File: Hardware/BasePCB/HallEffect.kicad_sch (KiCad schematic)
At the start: 4 parts, among them IC3 TMCS1123C1AQDVGR

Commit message: add JLC p/n
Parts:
- C5: Assemble (none) -> Y; LSCC P/N (none) -> C14663
- IC3: Assemble (none) -> Y; LSCC P/N (none) -> C22445470
- R2: Assemble (none) -> Y; LSCC P/N (none) -> C25804
- TP27: Assemble (none) -> N
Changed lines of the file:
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@@
+			)
+		)
+		(property "LSCC P/N" ""
+			(at 149.86 77.47 0)
+			(effects
+				(font
+					(size 1.27 1.27)
+				)
+				(hide yes)
+			)
+		)
+		(property "Assemble" "N"
+			(at 149.86 77.47 0)
+			(effects
+				(font
+					(size 1.27 1.27)
+				)
+				(hide yes)
 			)
 		)
@@
 		)
 		(property "P/N" "MLASH168SB7104KTNA01"
+			(at 76.2 81.28 0)
+			(effects
+				(font
+					(size 1.27 1.27)
+				)
+				(hide yes)
+			)
+		)
+		(property "LSCC P/N" "C14663"
+			(at 76.2 81.28 0)
+			(effects
+				(font
+					(size 1.27 1.27)
+				)
+				(hide yes)
+			)
+		)
+		(property "Assemble" "Y"
 			(at 76.2 81.28 0)
 			(effects
@@
 			)
 		)
+		(property "LSCC P/N" "C22445470"
+			(at 104.14 72.39 0)
+			(effects
+				(font
+					(size 1.27 1.27)
+				)
+				(hide yes)
+			)
+		)
+		(property "Assemble" "Y"
+			(at 104.14 72.39 0)
+			(effects
+				(font
+					(size 1.27 1.27)
+				)
+				(hide yes)
+			)
+		)
 		(pin "7"
 		)
@@
 			(at 87.63 81.28 0)
 			(effects
+				(font
+					(size 1.27 1.27)
+				)
+				(hide yes)
+			)
+		)
+		(property "LSCC P/N" "C25804"
+			(at 87.63 81.28 0)
+			(effects
+				(font
+					(size 1.27 1.27)
+				)
+				(hide yes)
+			)
+		)
+		(property "Assemble" "Y"
+			(at 87.63 81.28 0)
+			(effects

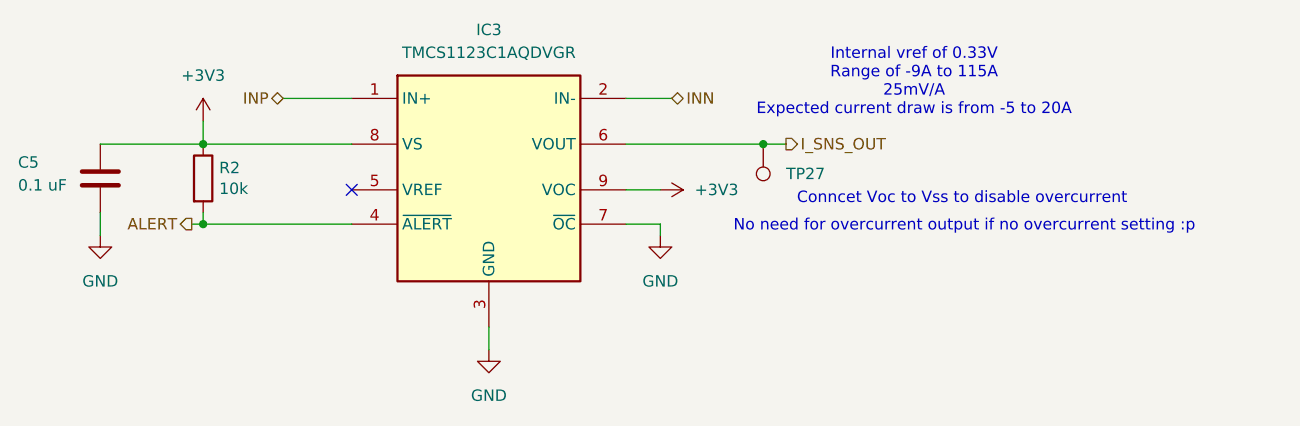
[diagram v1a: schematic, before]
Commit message: new hall effect IC
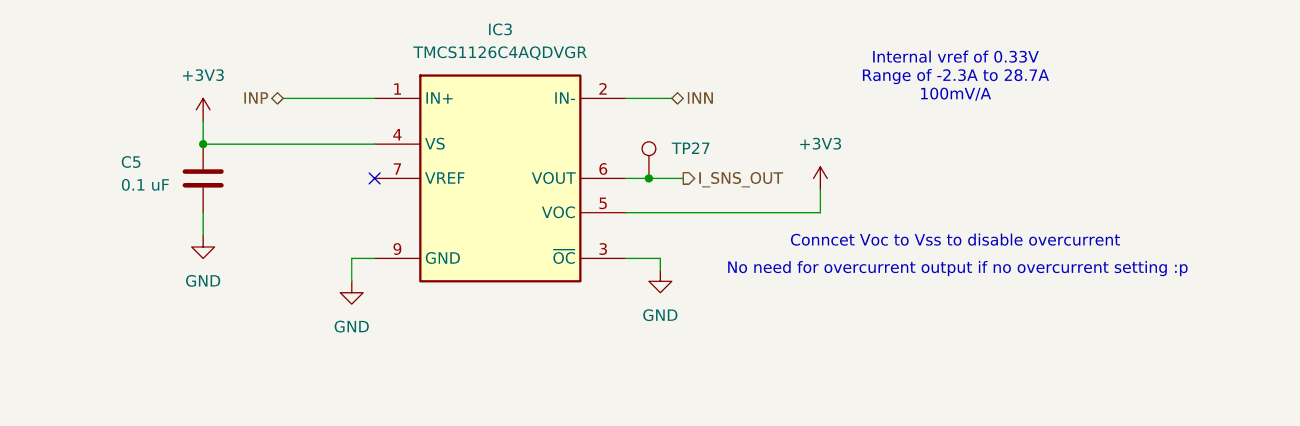
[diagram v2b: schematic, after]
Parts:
- removed IC3: TMCS1123C1AQDVGR, LV Carrier Library:TMCS1123C1AQDVGR, symbol LV-Carrier:TMCS1123C1AQDVGR
- removed R2: 10k, Resistor_SMD:R_0603_1608Metric_Pad0.98x0.95mm_HandSolder, symbol Device:R
- added IC3: TMCS1126C4AQDVGR, LV Carrier Library:TMCS1126C4AQDVGR, symbol LV-Carrier:TMCS1126C4AQDVGR
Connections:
- net +3V3: now also IC3.4 (VS), IC3.5 (VOC)
- net GND: now also IC3.3 (~{OC}), IC3.9 (GND)
- net INN: now also IC3.10 (NC_2), IC3.2 (IN-)
- net INP: now also IC3.1 (IN+)
- net I_SNS_OUT: now also IC3.6 (VOUT)
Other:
- note added: "Internal vref of 0.33V Range of -2.3A to 28.7A 100mV/A"
- note removed: "Internal vref of 0.33V Range of -9A to 115A 25mV/A Expected current draw is from -5 to 20A"
- moved on the sheet: C5, TP27

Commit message: lil shah pt 3
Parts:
- C5: LSCC P/N C14663 -> (none); LSCS P/N (none) -> C14663
- IC3: LSC P/N C37878146 -> (none); LSCS P/N (none) -> C37878146
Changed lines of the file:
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@@
-			)
-		)
-		(property "LSCC P/N" ""
-			(at 137.16 81.28 0)
-			(effects
-				(font
-					(size 1.27 1.27)
-				)
-				(hide yes)
 			)
 		)
@@
 			)
 		)
-		(property "LSCC P/N" "C14663"
-			(at 87.63 81.28 0)
-			(effects
-				(font
-					(size 1.27 1.27)
-				)
-				(hide yes)
-			)
-		)
 		(property "Assemble" "Y"
+			(at 87.63 81.28 0)
+			(effects
+				(font
+					(size 1.27 1.27)
+				)
+				(hide yes)
+			)
+		)
+		(property "LSCS P/N" "C14663"
 			(at 87.63 81.28 0)
 			(effects
@@
 			)
 		)
-		(property "LSC P/N" "C37878146"
+		(property "LSCS P/N" "C37878146"
 			(at 106.68 72.39 0)
 			(effects
